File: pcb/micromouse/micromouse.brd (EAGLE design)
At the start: 81.5 x 99.2 mm, 57 parts, among them J1 Connector_M1, J2 Connector_M2, J4 Programmer

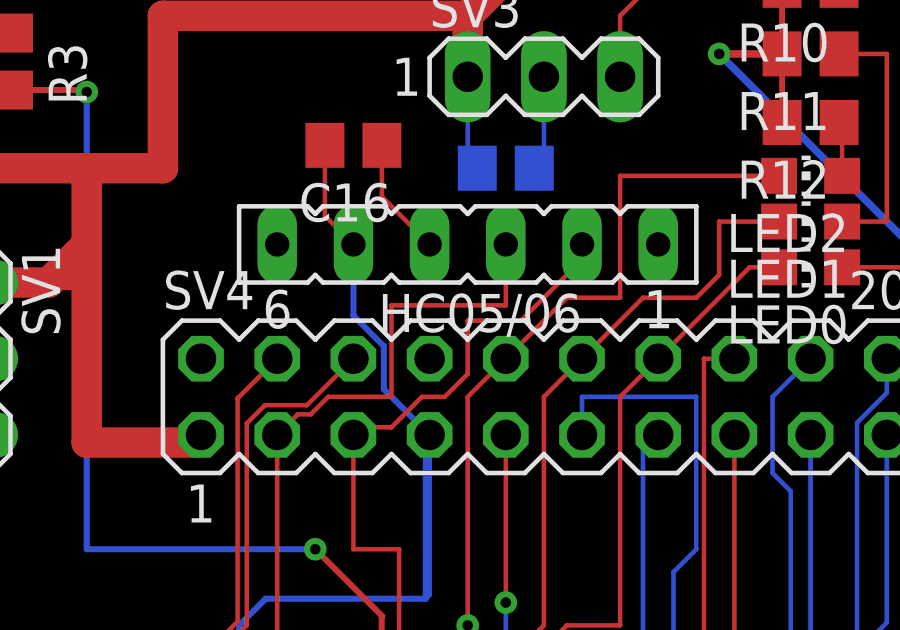
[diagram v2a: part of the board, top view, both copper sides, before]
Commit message: Remove resolved comments and only use resistors fom E12 series.
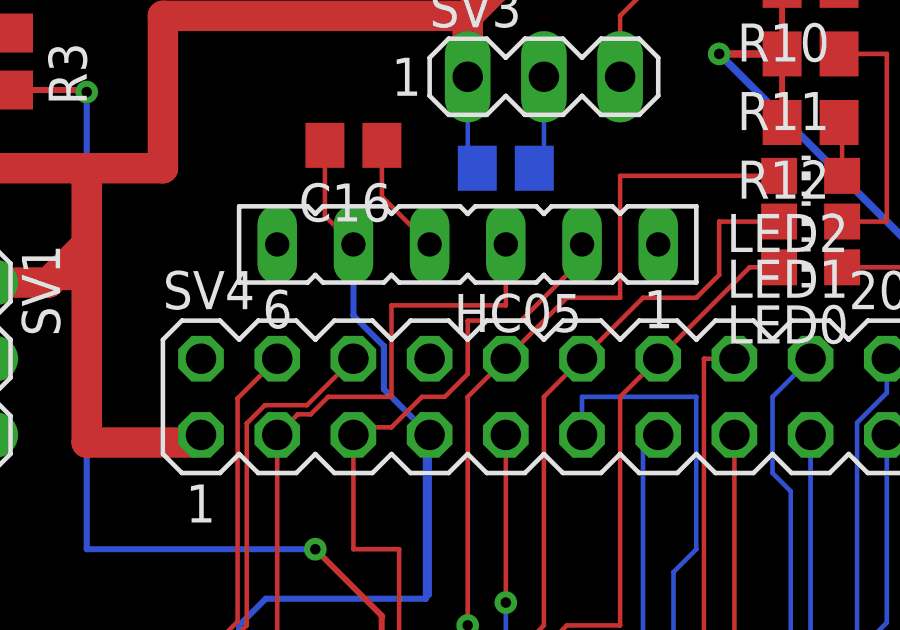
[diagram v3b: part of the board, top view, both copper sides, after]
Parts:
- R10, R11, R12: value 121 -> 120R
- R13, R14: value 10 -> 10R
- R3, R4, R8: value 10k -> 10kR
- R9: value 1k -> 1kR
- renumbered HC05/06 to HC05
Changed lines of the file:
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@@
 <attribute name="VALUE" x="53.086" y="46.101" size="1.778" layer="27" ratio="10" rot="R90"/>
 </element>
-<element name="HC05/06" library="con-lsta" library_urn="urn:adsk.eagle:library:161" package="FE06" package3d_urn="urn:adsk.eagle:package:8191/1" value="UART" x="38.1" y="78.74" smashed="yes" rot="R180">
+<element name="HC05" library="con-lsta" library_urn="urn:adsk.eagle:library:161" package="FE06" package3d_urn="urn:adsk.eagle:package:8191/1" value="UART" x="38.1" y="78.74" smashed="yes" rot="R180">
 <attribute name="MF" value="" x="-30.48" y="132.08" size="1.778" layer="27" rot="R180" display="off"/>
 <attribute name="MPN" value="" x="-30.48" y="132.08" size="1.778" layer="27" rot="R180" display="off"/>
@@
 <attribute name="VALUE" x="66.63" y="56.29" size="1.27" layer="27" rot="R90"/>
 </element>
-<element name="R10" library="rcl" library_urn="urn:adsk.eagle:library:334" package="R0805" package3d_urn="urn:adsk.eagle:package:23553/2" value="121" x="49.53" y="87.376" smashed="yes" rot="R180">
+<element name="R10" library="rcl" library_urn="urn:adsk.eagle:library:334" package="R0805" package3d_urn="urn:adsk.eagle:package:23553/2" value="120R" x="49.53" y="87.376" smashed="yes" rot="R180">
 <attribute name="NAME" x="50.165" y="86.106" size="1.27" layer="25" rot="R180"/>
 <attribute name="POPULARITY" value="86" x="-25.4" y="157.226" size="1.778" layer="27" rot="R180" display="off"/>
@@
 <attribute name="VALUE" x="50.165" y="89.916" size="1.27" layer="27" rot="R180"/>
 </element>
-<element name="R11" library="rcl" library_urn="urn:adsk.eagle:library:334" package="R0805" package3d_urn="urn:adsk.eagle:package:23553/2" value="121" x="49.53" y="85.09" smashed="yes" rot="R180">
+<element name="R11" library="rcl" library_urn="urn:adsk.eagle:library:334" package="R0805" package3d_urn="urn:adsk.eagle:package:23553/2" value="120R" x="49.53" y="85.09" smashed="yes" rot="R180">
 <attribute name="NAME" x="50.165" y="83.82" size="1.27" layer="25" rot="R180"/>
 <attribute name="POPULARITY" value="86" x="15.24" y="161.29" size="1.778" layer="27" rot="R180" display="off"/>
@@
 <attribute name="VALUE" x="50.165" y="87.63" size="1.27" layer="27" rot="R180"/>
 </element>
-<element name="R12" library="rcl" library_urn="urn:adsk.eagle:library:334" package="R0805" package3d_urn="urn:adsk.eagle:package:23553/2" value="121" x="49.53" y="82.804" smashed="yes" rot="R180">
+<element name="R12" library="rcl" library_urn="urn:adsk.eagle:library:334" package="R0805" package3d_urn="urn:adsk.eagle:package:23553/2" value="120R" x="49.53" y="82.804" smashed="yes" rot="R180">
 <attribute name="NAME" x="50.165" y="81.534" size="1.27" layer="25" rot="R180"/>
 <attribute name="POPULARITY" value="86" x="33.02" y="159.004" size="1.778" layer="27" rot="R180" display="off"/>
@@
 <attribute name="VALUE" x="50.165" y="85.344" size="1.27" layer="27" rot="R180"/>
 </element>
-<element name="R13" library="rcl" library_urn="urn:adsk.eagle:library:334" package="R0805" package3d_urn="urn:adsk.eagle:package:23553/2" value="10" x="32.258" y="45.466" smashed="yes" rot="MR90">
+<element name="R13" library="rcl" library_urn="urn:adsk.eagle:library:334" package="R0805" package3d_urn="urn:adsk.eagle:package:23553/2" value="10R" x="32.258" y="45.466" smashed="yes" rot="MR90">
 <attribute name="NAME" x="33.528" y="44.831" size="1.27" layer="26" rot="MR90"/>
 <attribute name="POPULARITY" value="86" x="-43.942" y="68.326" size="1.778" layer="28" rot="MR90" display="off"/>
@@
 <attribute name="VALUE" x="29.718" y="44.831" size="1.27" layer="28" rot="MR90"/>
 </element>
-<element name="R14" library="rcl" library_urn="urn:adsk.eagle:library:334" package="R0805" package3d_urn="urn:adsk.eagle:package:23553/2" value="10" x="44.704" y="44.958" smashed="yes" rot="MR90">
+<element name="R14" library="rcl" library_urn="urn:adsk.eagle:library:334" package="R0805" package3d_urn="urn:adsk.eagle:package:23553/2" value="10R" x="44.704" y="44.958" smashed="yes" rot="MR90">
 <attribute name="NAME" x="45.974" y="44.323" size="1.27" layer="26" rot="MR90"/>
 <attribute name="POPULARITY" value="86" x="-31.496" y="74.168" size="1.778" layer="28" rot="MR90" display="off"/>
@@
 <attribute name="VALUE" x="42.164" y="44.323" size="1.27" layer="28" rot="MR90"/>
 </element>
-<element name="R8" library="rcl" library_urn="urn:adsk.eagle:library:334" package="R0805" package3d_urn="urn:adsk.eagle:package:23553/2" value="10k" x="77.216" y="72.136" smashed="yes">
+<element name="R8" library="rcl" library_urn="urn:adsk.eagle:library:334" package="R0805" package3d_urn="urn:adsk.eagle:package:23553/2" value="10kR" x="77.216" y="72.136" smashed="yes">
 <attribute name="NAME" x="76.581" y="73.406" size="1.27" layer="25"/>
 <attribute name="POPULARITY" value="86" x="116.586" y="-4.064" size="1.778" layer="27" display="off"/>
@@
 <attribute name="VALUE" x="76.581" y="69.596" size="1.27" layer="27"/>
 </element>
-<element name="R9" library="rcl" library_urn="urn:adsk.eagle:library:334" package="R0805" package3d_urn="urn:adsk.eagle:package:23553/2" value="1k" x="77.216" y="74.676" smashed="yes" rot="R180">
+<element name="R9" library="rcl" library_urn="urn:adsk.eagle:library:334" package="R0805" package3d_urn="urn:adsk.eagle:package:23553/2" value="1kR" x="77.216" y="74.676" smashed="yes" rot="R180">
 <attribute name="NAME" x="77.851" y="73.406" size="1.27" layer="25" rot="R180"/>
 <attribute name="POPULARITY" value="86" x="32.766" y="150.876" size="1.778" layer="27" rot="R180" display="off"/>
@@
 <attribute name="VALUE" x="36.83" y="81.407" size="1.27" layer="27" ratio="10"/>
 </element>
-<element name="R3" library="rcl" library_urn="urn:adsk.eagle:library:334" package="R0805" package3d_urn="urn:adsk.eagle:package:23553/2" value="10k" x="22.86" y="84.836" smashed="yes" rot="R270">
+<element name="R3" library="rcl" library_urn="urn:adsk.eagle:library:334" package="R0805" package3d_urn="urn:adsk.eagle:package:23553/2" value="10kR" x="22.86" y="84.836" smashed="yes" rot="R270">
 <attribute name="NAME" x="24.13" y="85.471" size="1.27" layer="25" rot="R270"/>
 <attribute name="POPULARITY" value="86" x="33.02" y="91.186" size="1.778" layer="27" rot="R270" display="off"/>
@@
 <attribute name="VALUE" x="20.574" y="84.582" size="1.27" layer="27" ratio="10" rot="R90"/>
 </element>
-<element name="R4" library="rcl" library_urn="urn:adsk.eagle:library:334" package="R0805" package3d_urn="urn:adsk.eagle:package:23553/2" value="10k" x="71.12" y="79.756" smashed="yes" rot="R90">
+<element name="R4" library="rcl" library_urn="urn:adsk.eagle:library:334" package="R0805" package3d_urn="urn:adsk.eagle:package:23553/2" value="10kR" x="71.12" y="79.756" smashed="yes" rot="R90">
 <attribute name="NAME" x="69.85" y="79.121" size="1.27" layer="25" rot="R90"/>
 <attribute name="POPULARITY" value="86" x="60.96" y="79.756" size="1.778" layer="27" rot="R90" display="off"/>
@@
 <contactref element="SV2" pad="2"/>
 <contactref element="SV3" pad="2"/>
-<contactref element="HC05/06" pad="4"/>
+<contactref element="HC05" pad="4"/>
 <contactref element="C16" pad="1"/>
 <contactref element="-" pad="B3,0"/>
@@
 <contactref element="BTN_1" pad="1"/>
 <contactref element="BTN_2" pad="1"/>
-<contactref element="HC05/06" pad="5"/>
+<contactref element="HC05" pad="5"/>
 <contactref element="C16" pad="2"/>
 <contactref element="J1" pad="4"/>
@@
 <signal name="TX">
 <contactref element="MICROCONTROLLER" pad="44"/>
-<contactref element="HC05/06" pad="2"/>
+<contactref element="HC05" pad="2"/>
 <contactref element="SV4" pad="5"/>
 <wire x1="36.64" y1="60.41" x2="35.814" y2="61.236" width="0.1524" layer="1"/>
@@
 <signal name="RX">
 <contactref element="MICROCONTROLLER" pad="1"/>
-<contactref element="HC05/06" pad="3"/>
+<contactref element="HC05" pad="3"/>
 <contactref element="SV4" pad="3"/>
 <wire x1="34.84" y1="58.61" x2="34.798" y2="58.652" width="0.1524" layer="1"/>

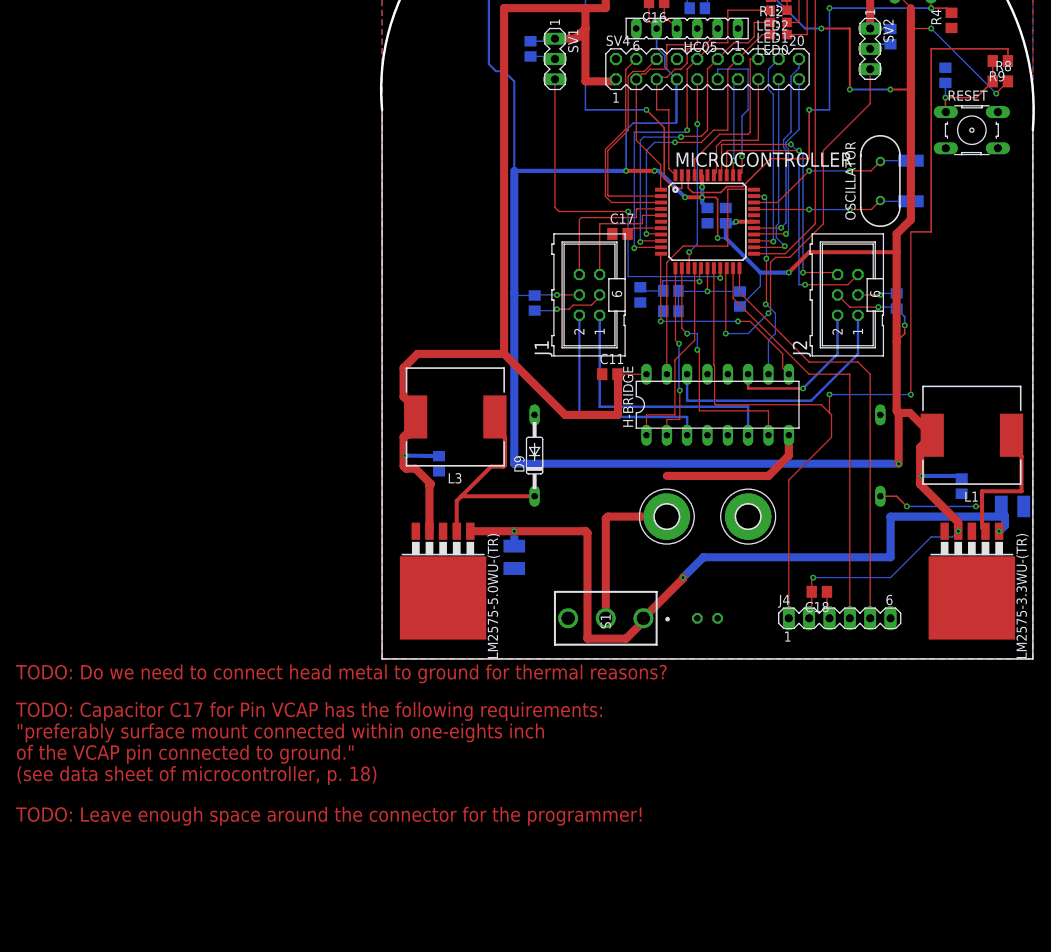
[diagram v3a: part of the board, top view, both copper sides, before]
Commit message: Use pin header as battery connector and change reset botton setup.
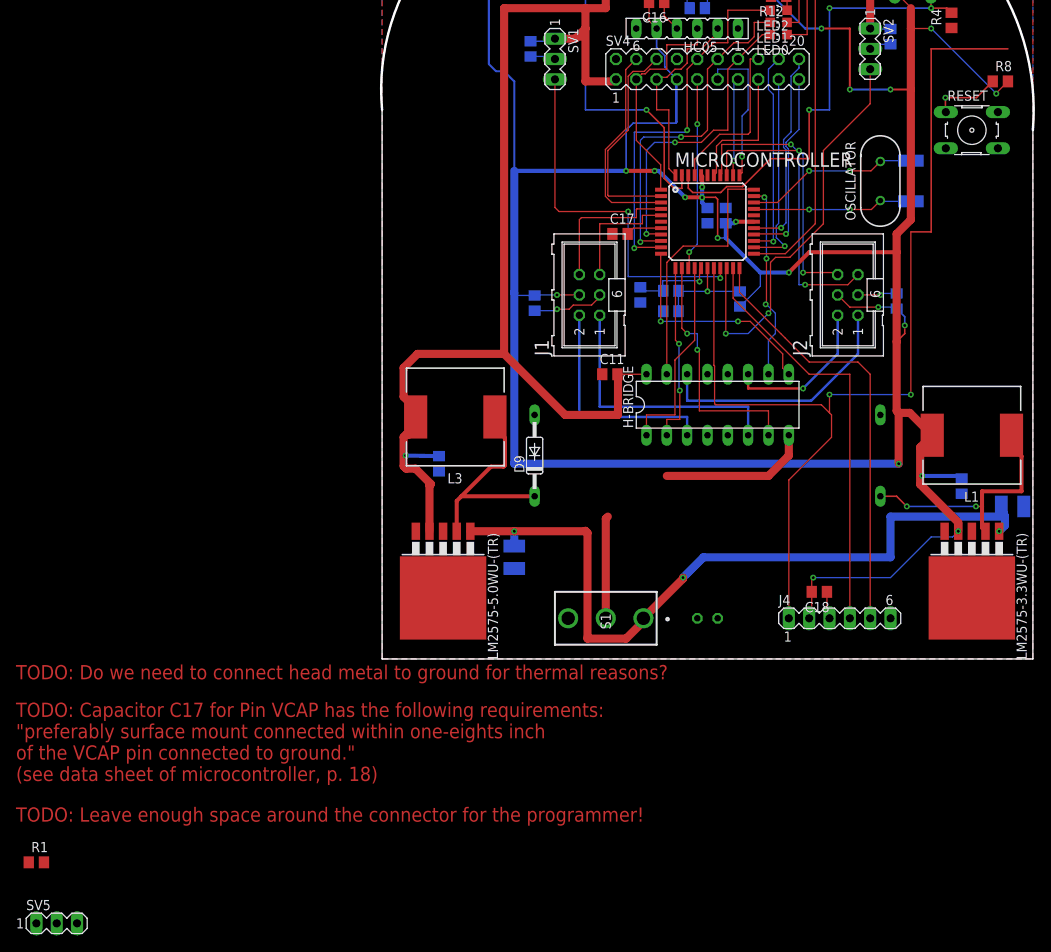
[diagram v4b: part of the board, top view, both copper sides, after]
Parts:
- removed +9V, -: Battery, holes:3,0-PAD
- removed C10: 100nF, rcl:C0805
- removed R9: 1kR, rcl:R0805
- added R1: 1kR, rcl:R0805
- added SV5: Battery connector, con-lstb:MA03-1
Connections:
- removed net N$1: C10.2, R8.1, R9.2, RESET.1
- net GND: now also SV5.1; no longer -.B3,0, C10.1
- net N$2: now also SV5.3; no longer +9V.B3,0
- net N_MCLR: now also R1.1, R1.2, R8.1, RESET.1; no longer R9.1
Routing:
- net N$1: track 13.0 -> 0.00 mm, vias 1 -> 0
- net N$2: track 20.2 -> 12.8 mm
- net N_MCLR: track 129.0 -> 136.2 mm, vias 2 -> 3

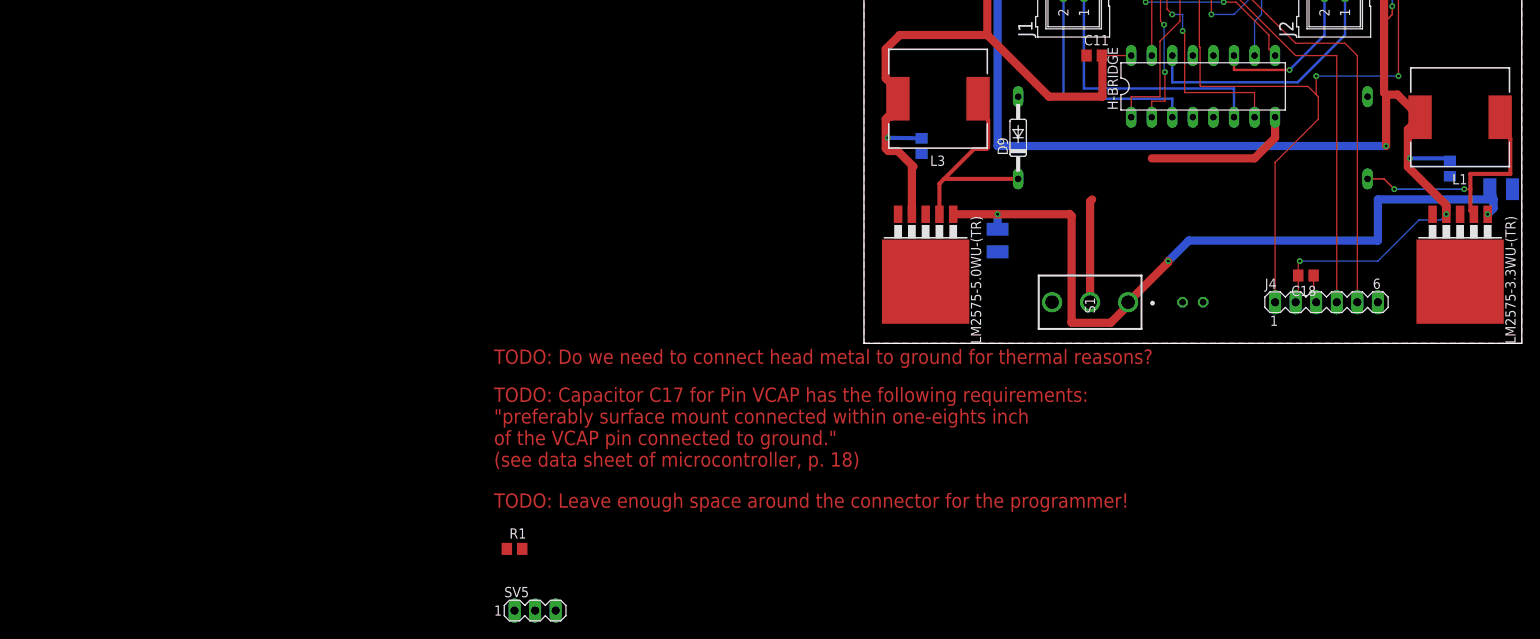
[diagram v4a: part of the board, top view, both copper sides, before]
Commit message: Exchanged capacitors and inductances in power supply
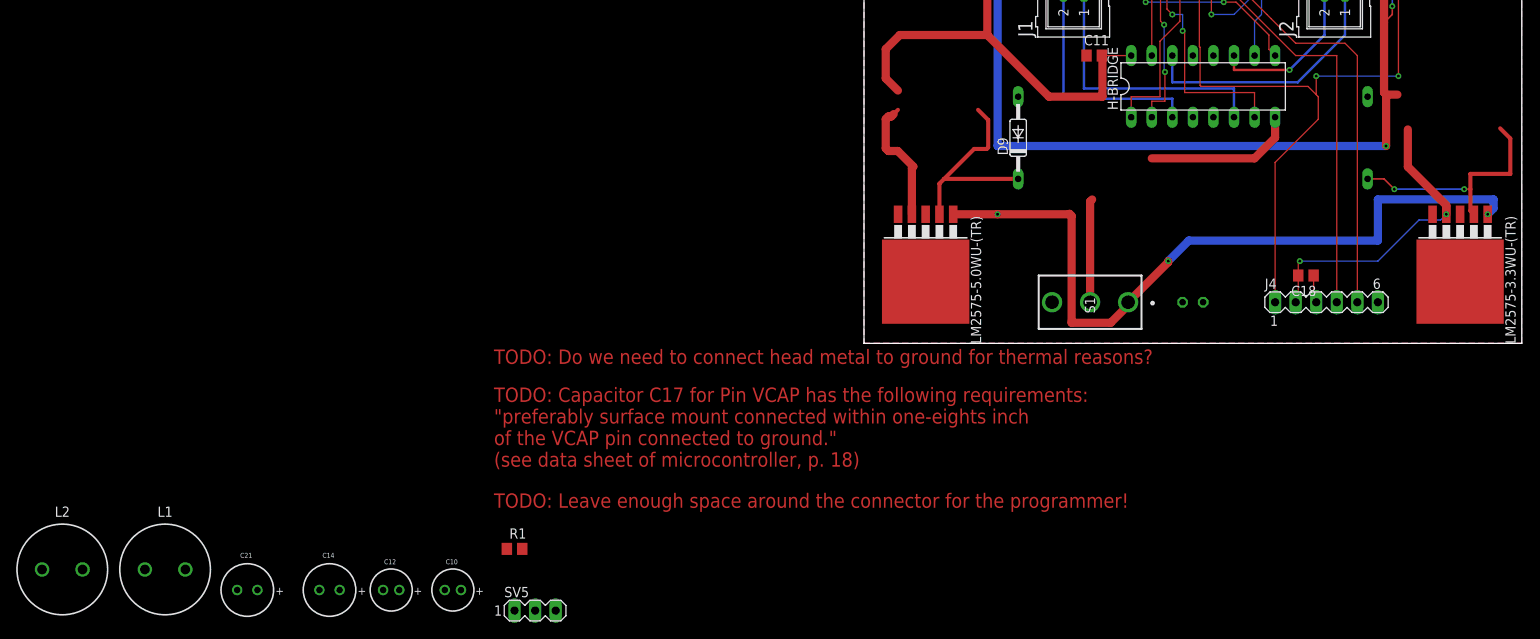
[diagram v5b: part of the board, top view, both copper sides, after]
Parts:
- removed C13, C15: 330uF, rcl:C0805
- removed L3: 330uH, Eagle_WE-PD (rev20a):WE-PD_1210
- added C10: 100 uF, Eagle_WCAP-ATG5 (rev21a):WCAP-ATG5_5X11(DXL)
- added C21: 330 uF, Eagle_WCAP-ATG5 (rev21a):WCAP-ATG5_6.3X11(DXL)
- added L2: 330uH, Eagle_WE-TIS (rev22a):WE-TIS_1111
- C12: value 100uF -> 100 uF; device rcl:C1210 -> Eagle_WCAP-ATG5 (rev21a):WCAP-ATG5_5X11(DXL)
- C14: value 100uF -> 330 uF; device rcl:C1210 -> Eagle_WCAP-ATG5 (rev21a):WCAP-ATG5_6.3X11(DXL)
- L1: device Eagle_WE-PD (rev20a):WE-PD_1210 -> Eagle_WE-TIS (rev22a):WE-TIS_1111
- moved L1 169.5 mm to (-86.4, -27.9), turned to 0 degrees
- moved C14 153.0 mm to (-66.0, -30.5), flipped to the top
- moved C12 86.5 mm to (-58.4, -30.5), flipped to the top, turned to 0 degrees
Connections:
- net +3V3: now also C21.1, L2.2; no longer C15.2, L1.2
- net +5V: now also C14.1, L1.2; no longer C13.2, L3.2
- net +9V: now also C10.1, C12.1; no longer C12.2, C14.2
- net GND: now also C10.2, C12.2, C14.2, C21.2; no longer C12.1, C13.1, C14.1, C15.1
- net N$7: now also L1.1; no longer L3.1
- net N$8: now also L2.1; no longer L1.1
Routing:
- net +3V3: track 409.0 -> 397.9 mm, vias 21 -> 20
- net +5V: track 215.1 -> 208.6 mm, vias 1 -> 0
- net +9V: track 114.5 -> 111.0 mm
- net N$8: track 30.8 -> 29.5 mm
- net N$7: track 27.3 -> 26.0 mm
